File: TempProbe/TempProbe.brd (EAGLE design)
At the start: 18.4 x 13.3 mm, 15 parts, among them U2 ATTINY841

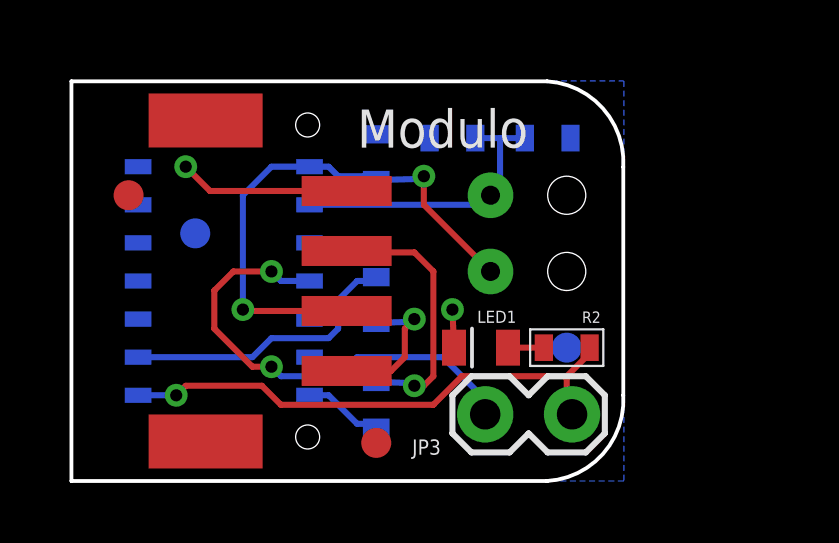
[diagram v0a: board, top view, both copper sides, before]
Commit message: Changed to use Grove connector
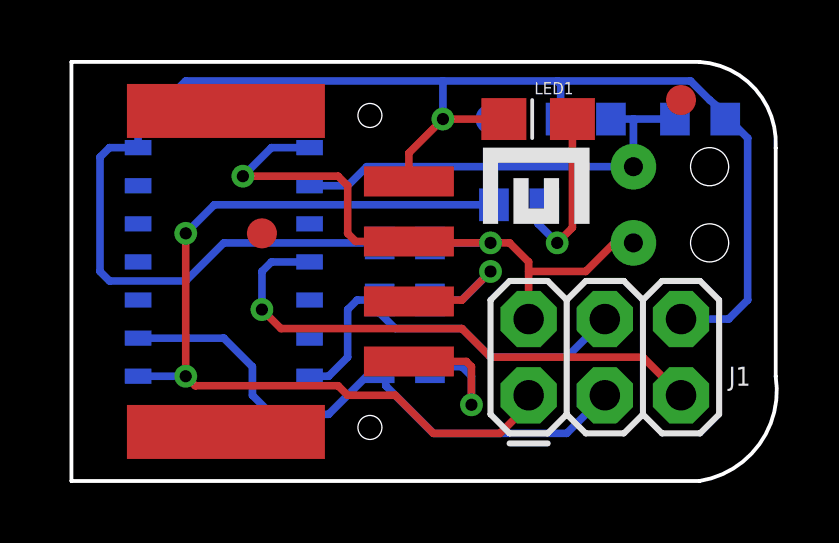
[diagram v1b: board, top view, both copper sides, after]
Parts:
- removed JP1: HEADER-1X4-JST-PA-SIDE-SMD, Modulo:JST-PA-SIDE-SMD
- removed JP3: M02LOCK, SparkFun-Connectors:1X02_LOCK
- added J1: AVR_SPI_PRG_6PTH, SparkFun-Connectors:2X3
- added JP2: HEADER-MODULO, Modulo:JST-PA-SIDE-SMD
- added U$1: (no value), Modulo:LOGO-TINY
- moved F1 18.7 mm to (20.3, 12.7)
- moved F4 12.1 mm to (4.76, 1.59)
- moved F2 10.6 mm to (14.0, 12.1)
- moved F3 7.96 mm to (6.35, 8.26)
- moved LED1 7.85 mm to (15.6, 12.1)
- moved C2 5.12 mm to (21.0, 12.1)
- moved R2 5.02 mm to (14.9, 9.21), flipped to the bottom
- moved PROBE1 4.86 mm to (20.0, 7.94)
- moved R1 4.49 mm to (17.1, 12.1)
- moved R9 3.62 mm to (11.1, 6.03), turned to 0 degrees
- moved C1 3.01 mm to (11.1, 7.94), turned to 0 degrees
- moved R8 2.42 mm to (11.1, 3.81), turned to 0 degrees
- moved U2 0.64 mm to (4.76, 11.1)
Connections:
- net GND: now also J1.6, JP2.1; no longer JP1.1
- net MISO/LED: now also J1.1; no longer JP3.1
- net RESET: now also J1.5; no longer JP3.2
- net SCL: now also JP2.4; no longer JP1.4
- net SCL/SCK: now also J1.3
- net SDA: now also JP2.3; no longer JP1.2
- net SDA/MOSI: now also J1.4
- net VCC: now also J1.2, JP2.2; no longer JP1.3
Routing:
- net GND: track 6.97 -> 52.8 mm, vias 2 -> 1
- net MISO/LED: track 17.7 -> 29.9 mm, vias 1 -> 2
- net SDA/MOSI: track 2.68 -> 13.4 mm
- net SCL/SCK: track 9.61 -> 19.5 mm
- net TEMP: track 9.85 -> 14.9 mm
- net N$2: track 1.20 -> 5.96 mm, vias 0 -> 1
- net VCC: track 18.0 -> 22.1 mm
- net SDA: track 8.74 -> 5.55 mm
- net RESET: track 15.9 -> 18.1 mm, vias 2 -> 1
- net SCL: track 4.84 -> 5.90 mm
- removed copper zone on layer 16, net GND
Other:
- board size 18.4 x 13.3 mm -> 23.5 x 14 mm
- board text added: "5"
- board text added: "Thermometer"
- board text removed: "Modulo"
- board text removed: "TempProbe v4"

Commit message: Changed to use direct wire soldering for modulo bus instead of a connector.
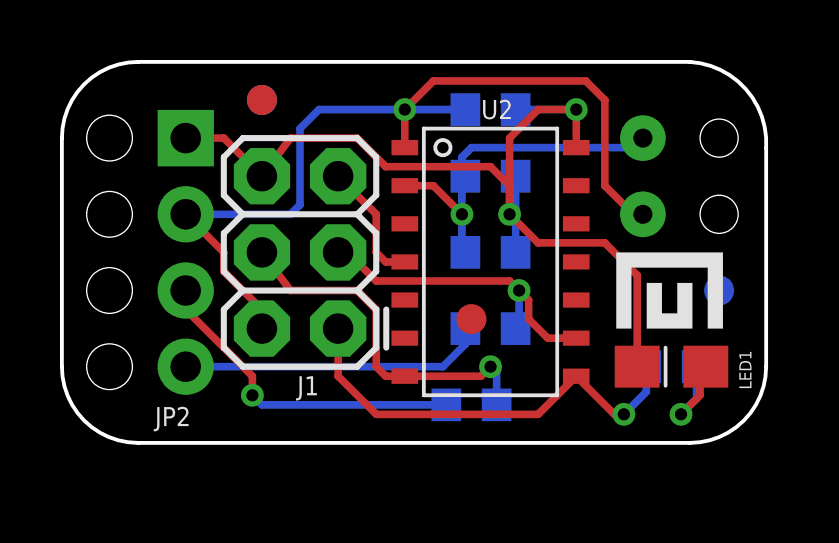
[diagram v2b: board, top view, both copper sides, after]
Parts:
- JP2: value HEADER-MODULO -> (none); device Modulo:JST-PA-SIDE-SMD -> SparkFun-Connectors:1X04_NO_SILK
- moved F4 11.2 mm to (6.35, 12.7)
- moved F1 10.1 mm to (13.3, 5.40)
- moved F2 9.52 mm to (21.6, 6.35)
- moved U2 9.52 mm to (14.3, 11.1), flipped to the top
- moved LED1 9.38 mm to (20.0, 3.81)
- moved C2 8.28 mm to (14.0, 7.62)
- moved R2 7.41 mm to (20.0, 3.81)
- moved J1 6.73 mm to (8.89, 5.08), turned to 90 degrees
- moved JP2 5.85 mm to (3.81, 11.4)
- moved U$1 5.65 mm to (19.7, 5.08)
- moved C1 5.28 mm to (14.0, 12.4), turned to 180 degrees
- moved F3 4.44 mm to (6.35, 12.7)
- moved R9 4.14 mm to (13.3, 2.54), turned to 180 degrees
- moved R1 3.70 mm to (14.0, 10.2), turned to 0 degrees
- moved R8 3.13 mm to (14.0, 5.08), turned to 180 degrees
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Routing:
- net GND: track 52.8 -> 32.9 mm, vias 1 -> 2
- net MISO/LED: track 29.9 -> 14.6 mm, vias 2 -> 1
- net RESET: track 18.1 -> 4.15 mm, vias 1 -> 0
- net SCL/SCK: track 19.5 -> 10.8 mm, vias 0 -> 1
- net VCC: track 22.1 -> 30.2 mm, vias 2 -> 1
- net SDA: track 5.55 -> 11.0 mm
- net SCL: track 5.90 -> 10.2 mm, vias 1 -> 0
- net TEMP: track 14.9 -> 11.9 mm, vias 0 -> 1
- net N$2: track 5.96 -> 3.91 mm
- net SDA/MOSI: track 13.4 -> 12.0 mm, vias 0 -> 1
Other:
- board size 23.5 x 14 mm -> 23.5 x 12.7 mm

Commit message: Various small tweaks based on testing and feedback from manufacturer.
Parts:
- R8, R9: value 150Ω -> 0Ω
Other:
- board text added: "Temperature Probe"
- board text removed: "Thermometer"
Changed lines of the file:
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@@
 <wire x1="23.1575" y1="3.81" x2="23.1575" y2="11.1" width="0.127" layer="20"/>
 <wire x1="23.1575" y1="11.1" x2="20.6175" y2="13.97" width="0.127" layer="20" curve="90"/>
-<text x="11.7475" y="5.715" size="1.016" layer="22" ratio="10" rot="SMR0">5</text>
-<text x="17.78" y="11.43" size="1.016" layer="22" ratio="10" rot="SMR270">Thermometer</text>
+<text x="20.32" y="5.08" size="1.016" layer="22" ratio="10" rot="SMR0">5</text>
+<text x="15.875" y="2.8575" size="1.016" layer="22" ratio="10" rot="SMR90">Temperature
+Probe</text>
 <hole x="1.27" y="11.43" drill="1.524"/>
 <hole x="1.27" y="8.89" drill="1.524"/>
@@
 <element name="C2" library="Modulo" package="0603" value=".1uF" x="13.97" y="7.62" smashed="yes" rot="MR0">
 <attribute name="PARTNUM" value="C0603C104K5RACTU" x="13.97" y="7.62" size="1.778" layer="28" rot="MR0" display="off"/>
-<attribute name="NAME" x="15.4305" y="7.4295" size="0.4064" layer="26" font="vector" rot="MR180"/>
+<attribute name="NAME" x="15.4305" y="8.0645" size="0.4064" layer="26" font="vector" rot="MR180"/>
 <attribute name="VALUE" value=".1uF" x="12.446" y="7.1755" size="0.4064" layer="28" font="vector" rot="MR0"/>
 </element>
@@
 <attribute name="PARTNUM" value="ATTINY841-SSUR" x="14.2875" y="11.1125" size="1.778" layer="27" rot="R270" display="off"/>
 </element>
-<element name="R8" library="Modulo" package="0603" value="150Ω" x="13.97" y="5.08" smashed="yes" rot="MR180">
-<attribute name="PARTNUM" value="ERJ-3EKF1500V" x="13.97" y="0" size="1.778" layer="28" rot="MR180" display="off"/>
-<attribute name="NAME" x="15.4305" y="5.5245" size="0.4064" layer="26" font="vector" rot="MR180"/>
-<attribute name="VALUE" x="12.446" y="4.6355" size="0.4064" layer="28" font="vector" rot="MR0"/>
+<element name="R8" library="Modulo" package="0603" value="0Ω" x="13.97" y="5.08" smashed="yes" rot="MR180">
+<attribute name="PARTNUM" value="ERJ-3GEY0R00V" x="13.97" y="0" size="1.778" layer="28" rot="MR180" display="off"/>
+<attribute name="NAME" x="14.7955" y="4.2545" size="0.4064" layer="26" font="vector" rot="MR180"/>
+<attribute name="VALUE" value="0Ω" x="12.446" y="4.6355" size="0.4064" layer="28" font="vector" rot="MR0"/>
 <attribute name="BOM" value="EXCLUDE" x="13.97" y="5.08" size="1.778" layer="28" rot="MR180" display="off"/>
 </element>
-<element name="R9" library="Modulo" package="0603" value="150Ω" x="13.335" y="2.54" smashed="yes" rot="MR180">
-<attribute name="PARTNUM" value="ERJ-3EKF1500V" x="9.525" y="1.27" size="1.778" layer="28" rot="MR180" display="off"/>
+<element name="R9" library="Modulo" package="0603" value="0Ω" x="13.335" y="2.54" smashed="yes" rot="MR180">
+<attribute name="PARTNUM" value="ERJ-3GEY0R00V" x="9.525" y="1.27" size="1.778" layer="28" rot="MR180" display="off"/>
 <attribute name="NAME" x="11.8745" y="2.0955" size="0.4064" layer="26" font="vector" rot="MR0"/>
-<attribute name="VALUE" x="14.859" y="2.3495" size="0.4064" layer="28" font="vector" rot="MR180"/>
+<attribute name="VALUE" value="0Ω" x="14.859" y="2.3495" size="0.4064" layer="28" font="vector" rot="MR180"/>
 <attribute name="BOM" value="EXCLUDE" x="13.335" y="2.54" size="1.778" layer="28" rot="MR180" display="off"/>
 </element>
@@
 </board>
 </drawing>
+<compatibility>
+<note version="6.3" minversion="6.2.2" severity="warning">
+Since Version 6.2.2 text objects can contain more than one line,
+which will not be processed correctly with this version.
+</note>
+</compatibility>
 </eagle>

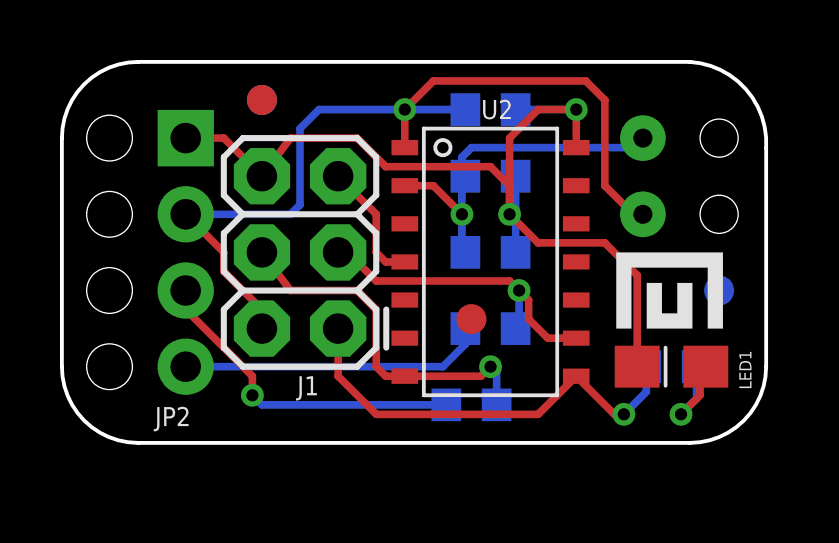
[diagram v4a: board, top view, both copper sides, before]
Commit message: Various minor tweaks based on testing and feedback from manufacturer
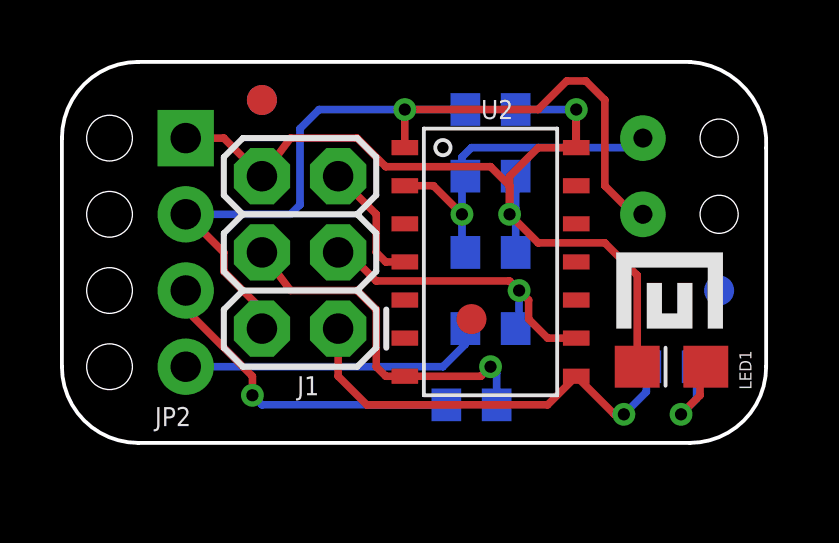
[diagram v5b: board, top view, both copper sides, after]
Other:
- board text added: "6"
- board text removed: "5"

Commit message: Added unique board prefixes to part numbers due to CM requirements
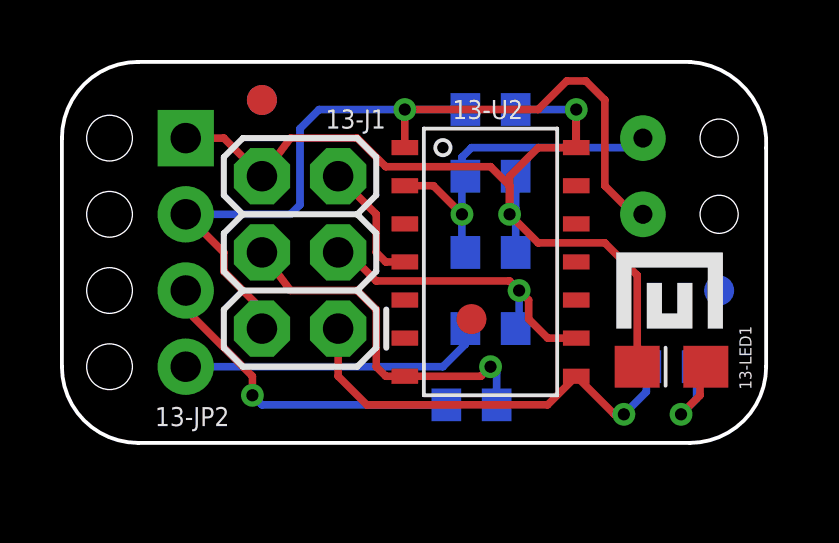
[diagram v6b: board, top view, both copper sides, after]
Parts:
- removed F3, F4: FIDUCIAL, Modulo:FIDUCIAL_1MM
- added 13-F3, 13-F4: FIDUCIAL, Modulo:FIDUCIAL_1MM
- renumbered C1 to 13-C1, C2 to 13-C2, F1 to 13-F1, F2 to 13-F2, J1 to 13-J1, JP2 to 13-JP2, LED1 to 13-LED1, PROBE1 to 13-PROBE1, R1 to 13-R1, R2 to 13-R2, R8 to 13-R8, R9 to 13-R9, U2 to 13-U2
